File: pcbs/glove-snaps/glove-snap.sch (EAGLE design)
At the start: 4 parts

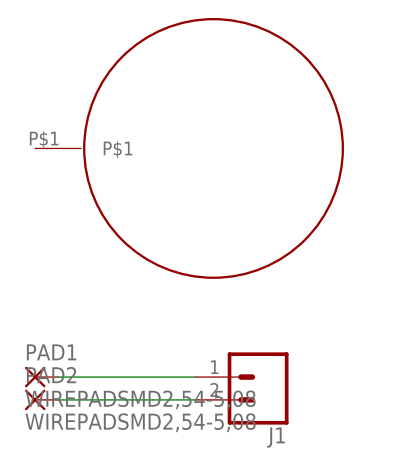
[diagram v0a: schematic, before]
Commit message: Update bom and exported schematics
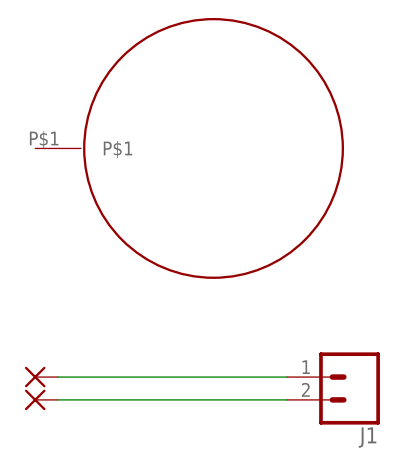
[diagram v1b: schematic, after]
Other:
- moved on the sheet: J1
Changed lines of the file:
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@@
 </plain>
 <instances>
-<instance part="J1" gate="G$1" x="109.22" y="86.36" smashed="yes" rot="R180">
-<attribute name="VALUE" x="111.76" y="91.186" size="1.778" layer="96" font="vector" rot="R180"/>
-<attribute name="NAME" x="111.76" y="80.772" size="1.778" layer="95" font="vector" rot="R180"/>
+<instance part="J1" gate="G$1" x="119.38" y="86.36" smashed="yes" rot="R180">
+<attribute name="VALUE" x="121.92" y="91.186" size="1.778" layer="96" font="vector" rot="R180"/>
+<attribute name="NAME" x="121.92" y="80.772" size="1.778" layer="95" font="vector" rot="R180"/>
 </instance>
-<instance part="PAD1" gate="G$1" x="83.82" y="86.36" smashed="yes">
-<attribute name="NAME" x="82.677" y="88.2142" size="1.778" layer="95"/>
-<attribute name="VALUE" x="82.677" y="83.058" size="1.778" layer="96"/>
-</instance>
-<instance part="PAD2" gate="G$1" x="83.82" y="83.82" smashed="yes">
-<attribute name="NAME" x="82.677" y="85.6742" size="1.778" layer="95"/>
-<attribute name="VALUE" x="82.677" y="80.518" size="1.778" layer="96"/>
-</instance>
+<instance part="PAD1" gate="G$1" x="83.82" y="86.36" smashed="yes"/>
+<instance part="PAD2" gate="G$1" x="83.82" y="83.82" smashed="yes"/>
 <instance part="U$1" gate="G$1" x="83.82" y="111.76" smashed="yes"/>
 </instances>
@@
 <pinref part="PAD1" gate="G$1" pin="P"/>
 <pinref part="J1" gate="G$1" pin="1"/>
-<wire x1="101.6" y1="86.36" x2="86.36" y2="86.36" width="0.1524" layer="91"/>
+<wire x1="111.76" y1="86.36" x2="86.36" y2="86.36" width="0.1524" layer="91"/>
 </segment>
 </net>
@@
 <pinref part="J1" gate="G$1" pin="2"/>
 <pinref part="PAD2" gate="G$1" pin="P"/>
-<wire x1="86.36" y1="83.82" x2="101.6" y2="83.82" width="0.1524" layer="91"/>
+<wire x1="86.36" y1="83.82" x2="111.76" y2="83.82" width="0.1524" layer="91"/>
 </segment>
 </net>
